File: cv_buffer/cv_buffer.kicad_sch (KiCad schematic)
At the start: 8 parts, among them J1 CV connector, J2 Pot connector, U1 HT7550-1, U2 TLV6001UIDBVR

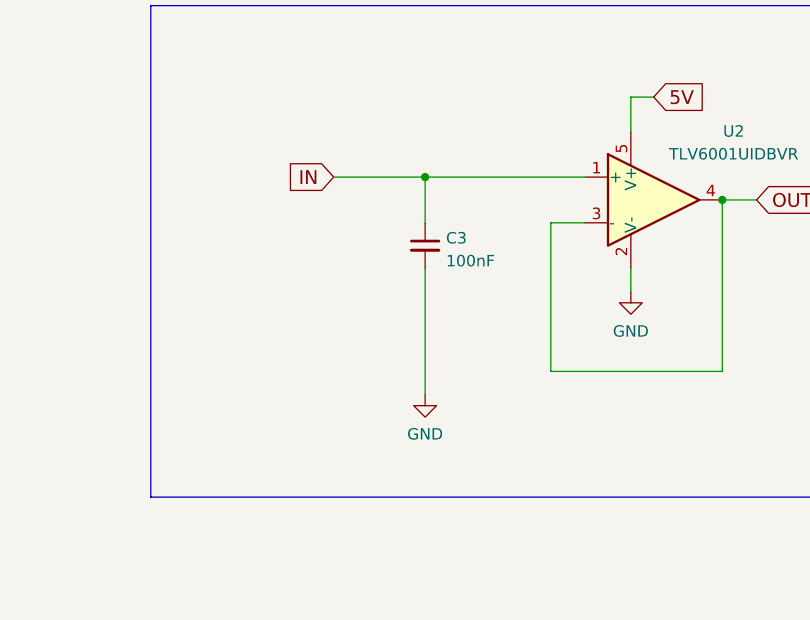
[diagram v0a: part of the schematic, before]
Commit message: - added tapering resistor - added fabrication script
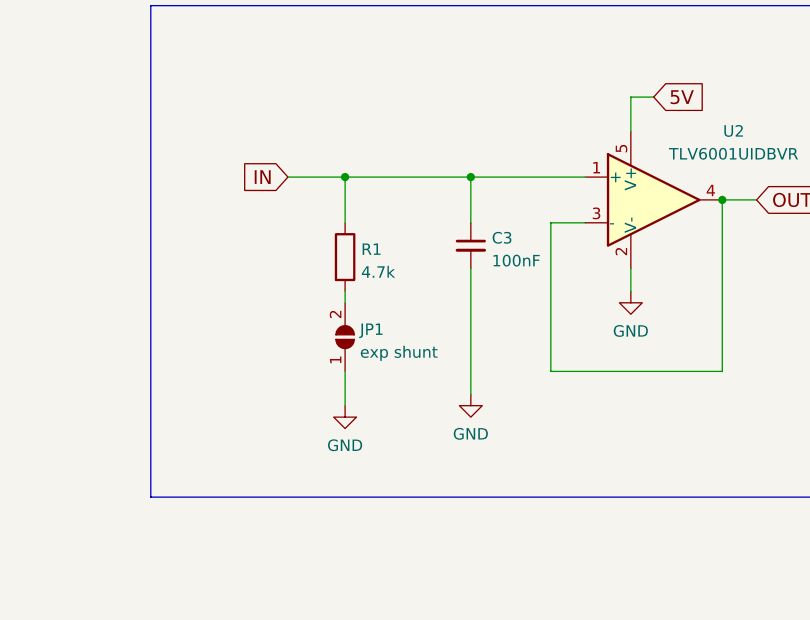
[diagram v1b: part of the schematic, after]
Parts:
- added JP1: exp shunt, Jumper:SolderJumper-2_P1.3mm_Open_TrianglePad1.0x1.5mm, symbol Jumper:SolderJumper_2_Open
- added R1: 4.7k, Resistor_SMD:R_0402_1005Metric, symbol Device:R
- U1: JLCPCB_CORRECTION (none) -> 0;0;180
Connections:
- net GND: now also JP1.1 (A)
- net IN: now also R1.1
- new net: JP1.2 (B), R1.2
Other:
- moved on the sheet: C3
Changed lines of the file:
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@@
   (junction (at 99.06 48.26) (diameter 0) (color 0 0 0 0)
   )
+  (junction (at 100.33 101.6) (diameter 0) (color 0 0 0 0)
+  )
   (junction (at 142.24 104.14) (diameter 0) (color 0 0 0 0)
   )
   (junction (at 120.65 59.69) (diameter 0) (color 0 0 0 0)
   )
-  (junction (at 109.22 101.6) (diameter 0) (color 0 0 0 0)
+  (junction (at 114.3 101.6) (diameter 0) (color 0 0 0 0)
   )
   (polyline (pts (xy 78.74 82.55) (xy 78.74 137.16))
@@
     (stroke (width 0) (type default) (color 0 0 0 0))
   )
+  (wire (pts (xy 100.33 101.6) (xy 100.33 106.68))
+    (stroke (width 0) (type default) (color 0 0 0 0))
+  )
   (polyline (pts (xy 179.07 82.55) (xy 217.17 82.55))
     (stroke (width 0) (type default) (color 0 0 0 0))
@@
     (stroke (width 0) (type default) (color 0 0 0 0))
   )
+  (wire (pts (xy 100.33 114.3) (xy 100.33 115.57))
+    (stroke (width 0) (type default) (color 0 0 0 0))
+  )
   (wire (pts (xy 120.65 48.26) (xy 120.65 52.07))
     (stroke (width 0) (type default) (color 0 0 0 0))
@@
     (stroke (width 0) (type default) (color 0 0 0 0))
   )
-  (wire (pts (xy 109.22 111.76) (xy 109.22 125.73))
+  (wire (pts (xy 114.3 111.76) (xy 114.3 125.73))
+    (stroke (width 0) (type default) (color 0 0 0 0))
+  )
+  (wire (pts (xy 100.33 123.19) (xy 100.33 127))
     (stroke (width 0) (type default) (color 0 0 0 0))
   )
@@
     (stroke (width 0) (type default) (color 0 0 0 0))
   )
-  (wire (pts (xy 109.22 101.6) (xy 127 101.6))
+  (wire (pts (xy 114.3 101.6) (xy 127 101.6))
     (stroke (width 0) (type default) (color 0 0 0 0))
   )
@@
     (stroke (width 0) (type default) (color 0 0 0 0))
   )
-  (wire (pts (xy 109.22 101.6) (xy 109.22 106.68))
+  (wire (pts (xy 114.3 101.6) (xy 114.3 106.68))
     (stroke (width 0) (type default) (color 0 0 0 0))
   )
@@
     (stroke (width 0) (type default) (color 0 0 0 0))
   )
+  (wire (pts (xy 100.33 101.6) (xy 114.3 101.6))
+    (stroke (width 0) (type default) (color 0 0 0 0))
+  )
   (wire (pts (xy 132.08 92.71) (xy 134.62 92.71))
     (stroke (width 0) (type default) (color 0 0 0 0))
@@
     (stroke (width 0) (type default) (color 0 0 0 0))
   )
-  (wire (pts (xy 99.06 101.6) (xy 109.22 101.6))
+  (wire (pts (xy 93.98 101.6) (xy 100.33 101.6))
     (stroke (width 0) (type default) (color 0 0 0 0))
   )
@@
     )
   )
-  (global_label "IN" (shape input) (at 99.06 101.6 180) (fields_autoplaced)
-    (effects (font (size 1.524 1.524)) (justify right))
-    (property "Intersheet References" "${INTERSHEET_REFS}" (id 0) (at 93.9488 101.5048 0)
+  (global_label "IN" (shape input) (at 93.98 101.6 180) (fields_autoplaced)
+    (effects (font (size 1.524 1.524)) (justify right))
+    (property "Intersheet References" "${INTERSHEET_REFS}" (id 0) (at 88.8688 101.5048 0)
       (effects (font (size 1.524 1.524)) (justify right) hide)
     )
@@
     (pin "1")
   )
+  (symbol (lib_id "Jumper:SolderJumper_2_Open") (at 100.33 119.38 90) (unit 1)
+    (in_bom yes) (on_board yes) (fields_autoplaced)
+    (property "Reference" "JP1" (id 0) (at 101.981 118.5453 90)
+      (effects (font (size 1.27 1.27)) (justify right))
+    )
+    (property "Value" "exp shunt" (id 1) (at 101.981 121.0822 90)
+      (effects (font (size 1.27 1.27)) (justify right))
+    )
+    (property "Footprint" "Jumper:SolderJumper-2_P1.3mm_Open_TrianglePad1.0x1.5mm" (id 2) (at 100.33 119.38 0)
+      (effects (font (size 1.27 1.27)) hide)
+    )
+    (property "Datasheet" "~" (id 3) (at 100.33 119.38 0)
+      (effects (font (size 1.27 1.27)) hide)
+    )
+    (pin "1")
+    (pin "2")
+  )
   (symbol (lib_id "power:PWR_FLAG") (at 124.46 59.69 180) (unit 1)
     (in_bom yes) (on_board yes) (fields_autoplaced)
@@
     (pin "1")
   )
-  (symbol (lib_id "power:GND") (at 109.22 125.73 0) (unit 1)
-    (in_bom yes) (on_board yes) (fields_autoplaced)
-    (property "Reference" "#PWR01" (id 0) (at 109.22 132.08 0)
-      (effects (font (size 1.27 1.27)) hide)
-    )
-    (property "Value" "GND" (id 1) (at 109.22 130.1734 0))
-    (property "Footprint" "" (id 2) (at 109.22 125.73 0)
-      (effects (font (size 1.27 1.27)) hide)
-    )
-    (property "Datasheet" "" (id 3) (at 109.22 125.73 0)
+  (symbol (lib_id "power:GND") (at 114.3 125.73 0) (unit 1)
+    (in_bom yes) (on_board yes) (fields_autoplaced)
+    (property "Reference" "#PWR01" (id 0) (at 114.3 132.08 0)
+      (effects (font (size 1.27 1.27)) hide)
+    )
+    (property "Value" "GND" (id 1) (at 114.3 130.1734 0))
+    (property "Footprint" "" (id 2) (at 114.3 125.73 0)
+      (effects (font (size 1.27 1.27)) hide)
+    )
+    (property "Datasheet" "" (id 3) (at 114.3 125.73 0)
       (effects (font (size 1.27 1.27)) hide)
     )
@@
     )
     (property "LCSC" "C15850" (id 4) (at 99.06 54.61 0)
+      (effects (font (size 1.524 1.524)) hide)
+    )
+    (pin "1")
+    (pin "2")
+  )
+  (symbol (lib_id "Device:R") (at 100.33 110.49 0) (unit 1)
+    (in_bom yes) (on_board yes) (fields_autoplaced)
+    (property "Reference" "R1" (id 0) (at 102.108 109.6553 0)
+      (effects (font (size 1.27 1.27)) (justify left))
+    )
+    (property "Value" "4.7k" (id 1) (at 102.108 112.1922 0)
+      (effects (font (size 1.27 1.27)) (justify left))
+    )
+    (property "Footprint" "Resistor_SMD:R_0402_1005Metric" (id 2) (at 98.552 110.49 90)
+      (effects (font (size 1.27 1.27)) hide)
+    )
+    (property "Datasheet" "~" (id 3) (at 100.33 110.49 0)
+      (effects (font (size 1.27 1.27)) hide)
+    )
+    (property "LCSC" "C25900" (id 4) (at 100.33 110.49 0)
       (effects (font (size 1.524 1.524)) hide)
     )
@@
       (effects (font (size 1.524 1.524)) hide)
     )
+    (property "JLCPCB_CORRECTION" "0;0;180" (id 5) (at 110.49 48.26 0)
+      (effects (font (size 1.524 1.524)) hide)
+    )
     (pin "1")
     (pin "2")
@@
     )
     (property "Datasheet" "~" (id 3) (at 99.06 44.45 0)
+      (effects (font (size 1.27 1.27)) hide)
+    )
+    (pin "1")
+  )
+  (symbol (lib_id "power:GND") (at 100.33 127 0) (unit 1)
+    (in_bom yes) (on_board yes) (fields_autoplaced)
+    (property "Reference" "#PWR03" (id 0) (at 100.33 133.35 0)
+      (effects (font (size 1.27 1.27)) hide)
+    )
+    (property "Value" "GND" (id 1) (at 100.33 131.4434 0))
+    (property "Footprint" "" (id 2) (at 100.33 127 0)
+      (effects (font (size 1.27 1.27)) hide)
+    )
+    (property "Datasheet" "" (id 3) (at 100.33 127 0)
       (effects (font (size 1.27 1.27)) hide)
     )
@@
     (pin "3")
   )
-  (symbol (lib_id "Device:C_Small") (at 109.22 109.22 0) (unit 1)
-    (in_bom yes) (on_board yes) (fields_autoplaced)
-    (property "Reference" "C3" (id 0) (at 111.5441 108.3916 0)
-      (effects (font (size 1.27 1.27)) (justify left))
-    )
-    (property "Value" "100nF" (id 1) (at 111.5441 110.9285 0)
-      (effects (font (size 1.27 1.27)) (justify left))
-    )
-    (property "Footprint" "Capacitor_SMD:C_0402_1005Metric" (id 2) (at 109.22 109.22 0)
-      (effects (font (size 1.27 1.27)) hide)
-    )
-    (property "Datasheet" "~" (id 3) (at 109.22 109.22 0)
-      (effects (font (size 1.27 1.27)) hide)
-    )
-    (property "LCSC" "C307331" (id 4) (at 109.22 109.22 0)
+  (symbol (lib_id "Device:C_Small") (at 114.3 109.22 0) (unit 1)
+    (in_bom yes) (on_board yes) (fields_autoplaced)
+    (property "Reference" "C3" (id 0) (at 116.6241 108.3916 0)
+      (effects (font (size 1.27 1.27)) (justify left))
+    )
+    (property "Value" "100nF" (id 1) (at 116.6241 110.9285 0)
+      (effects (font (size 1.27 1.27)) (justify left))
+    )
+    (property "Footprint" "Capacitor_SMD:C_0402_1005Metric" (id 2) (at 114.3 109.22 0)
+      (effects (font (size 1.27 1.27)) hide)
+    )
+    (property "Datasheet" "~" (id 3) (at 114.3 109.22 0)
+      (effects (font (size 1.27 1.27)) hide)
+    )
+    (property "LCSC" "C307331" (id 4) (at 114.3 109.22 0)
       (effects (font (size 1.524 1.524)) hide)
     )
@@
       (reference "#PWR02") (unit 1) (value "GND") (footprint "")
     )
+    (path "/c64623ea-1b89-43ec-92c6-a2d8ff19adad"
+      (reference "#PWR03") (unit 1) (value "GND") (footprint "")
+    )
     (path "/3e5b385e-4a64-4053-880e-e0031299a98c"
       (reference "#PWR05") (unit 1) (value "GND") (footprint "")
@@
       (reference "J2") (unit 1) (value "Pot connector") (footprint "cycfi_library:pin_header_1x3p_2.54mm_smd_horizontal")
     )
+    (path "/4d15044e-ba42-49c7-9385-a61cb67a80bd"
+      (reference "JP1") (unit 1) (value "exp shunt") (footprint "Jumper:SolderJumper-2_P1.3mm_Open_TrianglePad1.0x1.5mm")
+    )
+    (path "/92180a56-bc8d-4a49-8fe4-c3dc9309f11b"
+      (reference "R1") (unit 1) (value "4.7k") (footprint "Resistor_SMD:R_0402_1005Metric")
+    )
     (path "/b29e7a3c-8a61-4d5d-8478-053e45b60270"

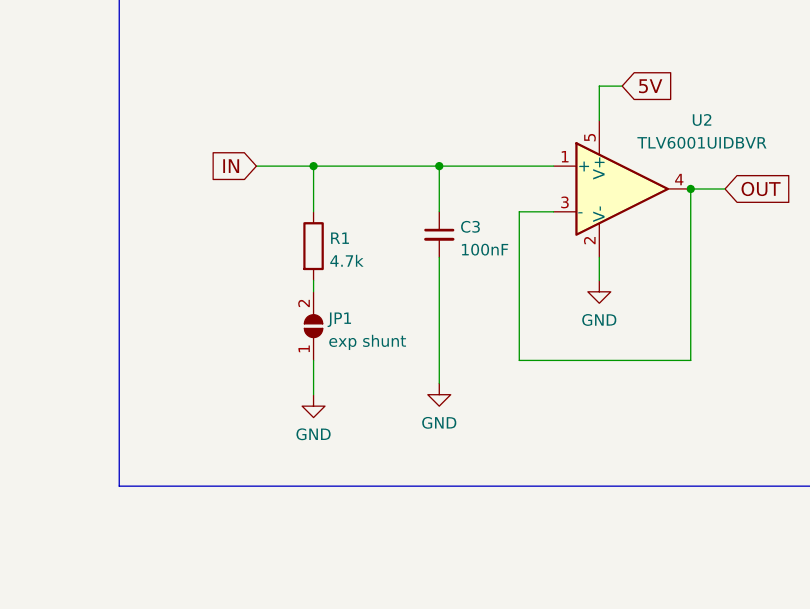
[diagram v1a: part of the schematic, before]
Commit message: Removed taper resistor
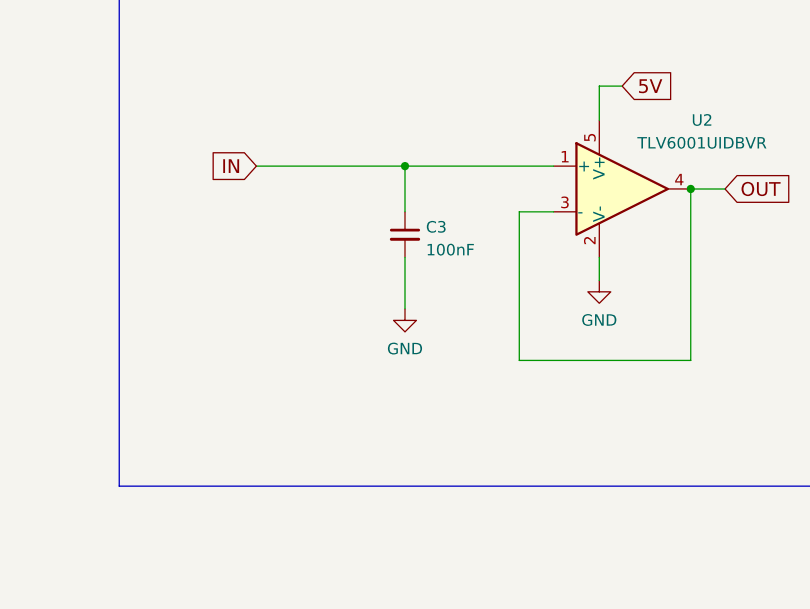
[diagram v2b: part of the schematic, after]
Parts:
- removed JP1: exp shunt, Jumper:SolderJumper-2_P1.3mm_Open_TrianglePad1.0x1.5mm, symbol Jumper:SolderJumper_2_Open
- removed R1: 4.7k, Resistor_SMD:R_0402_1005Metric, symbol Device:R
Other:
- moved on the sheet: C3
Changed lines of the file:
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@@
   (junction (at 99.06 48.26) (diameter 0) (color 0 0 0 0)
   )
-  (junction (at 100.33 101.6) (diameter 0) (color 0 0 0 0)
-  )
   (junction (at 142.24 104.14) (diameter 0) (color 0 0 0 0)
   )
   (junction (at 120.65 59.69) (diameter 0) (color 0 0 0 0)
   )
-  (junction (at 114.3 101.6) (diameter 0) (color 0 0 0 0)
+  (junction (at 110.49 101.6) (diameter 0) (color 0 0 0 0)
   )
   (polyline (pts (xy 78.74 82.55) (xy 78.74 137.16))
@@
     (stroke (width 0) (type default) (color 0 0 0 0))
   )
-  (wire (pts (xy 100.33 101.6) (xy 100.33 106.68))
-    (stroke (width 0) (type default) (color 0 0 0 0))
-  )
   (polyline (pts (xy 179.07 82.55) (xy 217.17 82.55))
     (stroke (width 0) (type default) (color 0 0 0 0))
@@
     (stroke (width 0) (type default) (color 0 0 0 0))
   )
-  (wire (pts (xy 100.33 114.3) (xy 100.33 115.57))
-    (stroke (width 0) (type default) (color 0 0 0 0))
-  )
   (wire (pts (xy 120.65 48.26) (xy 120.65 52.07))
     (stroke (width 0) (type default) (color 0 0 0 0))
@@
     (stroke (width 0) (type default) (color 0 0 0 0))
   )
-  (wire (pts (xy 114.3 111.76) (xy 114.3 125.73))
-    (stroke (width 0) (type default) (color 0 0 0 0))
-  )
-  (wire (pts (xy 100.33 123.19) (xy 100.33 127))
+  (wire (pts (xy 110.49 111.76) (xy 110.49 117.475))
     (stroke (width 0) (type default) (color 0 0 0 0))
   )
@@
     (stroke (width 0) (type default) (color 0 0 0 0))
   )
-  (wire (pts (xy 114.3 101.6) (xy 127 101.6))
+  (wire (pts (xy 110.49 101.6) (xy 127 101.6))
     (stroke (width 0) (type default) (color 0 0 0 0))
   )
@@
     (stroke (width 0) (type default) (color 0 0 0 0))
   )
-  (wire (pts (xy 114.3 101.6) (xy 114.3 106.68))
+  (wire (pts (xy 110.49 101.6) (xy 110.49 106.68))
     (stroke (width 0) (type default) (color 0 0 0 0))
   )
@@
     (stroke (width 0) (type default) (color 0 0 0 0))
   )
-  (wire (pts (xy 100.33 101.6) (xy 114.3 101.6))
+  (wire (pts (xy 93.98 101.6) (xy 110.49 101.6))
     (stroke (width 0) (type default) (color 0 0 0 0))
   )
@@
   )
   (polyline (pts (xy 138.43 35.56) (xy 138.43 73.66))
-    (stroke (width 0) (type default) (color 0 0 0 0))
-  )
-  (wire (pts (xy 93.98 101.6) (xy 100.33 101.6))
     (stroke (width 0) (type default) (color 0 0 0 0))
   )
@@
     (pin "1")
   )
-  (symbol (lib_id "Jumper:SolderJumper_2_Open") (at 100.33 119.38 90) (unit 1)
-    (in_bom yes) (on_board yes) (fields_autoplaced)
-    (property "Reference" "JP1" (id 0) (at 101.981 118.5453 90)
-      (effects (font (size 1.27 1.27)) (justify right))
-    )
-    (property "Value" "exp shunt" (id 1) (at 101.981 121.0822 90)
-      (effects (font (size 1.27 1.27)) (justify right))
-    )
-    (property "Footprint" "Jumper:SolderJumper-2_P1.3mm_Open_TrianglePad1.0x1.5mm" (id 2) (at 100.33 119.38 0)
-      (effects (font (size 1.27 1.27)) hide)
-    )
-    (property "Datasheet" "~" (id 3) (at 100.33 119.38 0)
-      (effects (font (size 1.27 1.27)) hide)
-    )
-    (pin "1")
-    (pin "2")
-  )
   (symbol (lib_id "power:PWR_FLAG") (at 124.46 59.69 180) (unit 1)
     (in_bom yes) (on_board yes) (fields_autoplaced)
@@
     (pin "1")
   )
-  (symbol (lib_id "power:GND") (at 114.3 125.73 0) (unit 1)
-    (in_bom yes) (on_board yes) (fields_autoplaced)
-    (property "Reference" "#PWR01" (id 0) (at 114.3 132.08 0)
-      (effects (font (size 1.27 1.27)) hide)
-    )
-    (property "Value" "GND" (id 1) (at 114.3 130.1734 0))
-    (property "Footprint" "" (id 2) (at 114.3 125.73 0)
-      (effects (font (size 1.27 1.27)) hide)
-    )
-    (property "Datasheet" "" (id 3) (at 114.3 125.73 0)
+  (symbol (lib_id "power:GND") (at 110.49 117.475 0) (unit 1)
+    (in_bom yes) (on_board yes) (fields_autoplaced)
+    (property "Reference" "#PWR01" (id 0) (at 110.49 123.825 0)
+      (effects (font (size 1.27 1.27)) hide)
+    )
+    (property "Value" "GND" (id 1) (at 110.49 121.9184 0))
+    (property "Footprint" "" (id 2) (at 110.49 117.475 0)
+      (effects (font (size 1.27 1.27)) hide)
+    )
+    (property "Datasheet" "" (id 3) (at 110.49 117.475 0)
       (effects (font (size 1.27 1.27)) hide)
     )
@@
     )
     (property "LCSC" "C15850" (id 4) (at 99.06 54.61 0)
-      (effects (font (size 1.524 1.524)) hide)
-    )
-    (pin "1")
-    (pin "2")
-  )
-  (symbol (lib_id "Device:R") (at 100.33 110.49 0) (unit 1)
-    (in_bom yes) (on_board yes) (fields_autoplaced)
-    (property "Reference" "R1" (id 0) (at 102.108 109.6553 0)
-      (effects (font (size 1.27 1.27)) (justify left))
-    )
-    (property "Value" "4.7k" (id 1) (at 102.108 112.1922 0)
-      (effects (font (size 1.27 1.27)) (justify left))
-    )
-    (property "Footprint" "Resistor_SMD:R_0402_1005Metric" (id 2) (at 98.552 110.49 90)
-      (effects (font (size 1.27 1.27)) hide)
-    )
-    (property "Datasheet" "~" (id 3) (at 100.33 110.49 0)
-      (effects (font (size 1.27 1.27)) hide)
-    )
-    (property "LCSC" "C25900" (id 4) (at 100.33 110.49 0)
       (effects (font (size 1.524 1.524)) hide)
     )
@@
     )
     (property "Datasheet" "~" (id 3) (at 99.06 44.45 0)
-      (effects (font (size 1.27 1.27)) hide)
-    )
-    (pin "1")
-  )
-  (symbol (lib_id "power:GND") (at 100.33 127 0) (unit 1)
-    (in_bom yes) (on_board yes) (fields_autoplaced)
-    (property "Reference" "#PWR03" (id 0) (at 100.33 133.35 0)
-      (effects (font (size 1.27 1.27)) hide)
-    )
-    (property "Value" "GND" (id 1) (at 100.33 131.4434 0))
-    (property "Footprint" "" (id 2) (at 100.33 127 0)
-      (effects (font (size 1.27 1.27)) hide)
-    )
-    (property "Datasheet" "" (id 3) (at 100.33 127 0)
       (effects (font (size 1.27 1.27)) hide)
     )
@@
     (pin "3")
   )
-  (symbol (lib_id "Device:C_Small") (at 114.3 109.22 0) (unit 1)
-    (in_bom yes) (on_board yes) (fields_autoplaced)
-    (property "Reference" "C3" (id 0) (at 116.6241 108.3916 0)
-      (effects (font (size 1.27 1.27)) (justify left))
-    )
-    (property "Value" "100nF" (id 1) (at 116.6241 110.9285 0)
-      (effects (font (size 1.27 1.27)) (justify left))
-    )
-    (property "Footprint" "Capacitor_SMD:C_0402_1005Metric" (id 2) (at 114.3 109.22 0)
-      (effects (font (size 1.27 1.27)) hide)
-    )
-    (property "Datasheet" "~" (id 3) (at 114.3 109.22 0)
-      (effects (font (size 1.27 1.27)) hide)
-    )
-    (property "LCSC" "C307331" (id 4) (at 114.3 109.22 0)
+  (symbol (lib_id "Device:C_Small") (at 110.49 109.22 0) (unit 1)
+    (in_bom yes) (on_board yes) (fields_autoplaced)
+    (property "Reference" "C3" (id 0) (at 112.8141 108.3916 0)
+      (effects (font (size 1.27 1.27)) (justify left))
+    )
+    (property "Value" "100nF" (id 1) (at 112.8141 110.9285 0)
+      (effects (font (size 1.27 1.27)) (justify left))
+    )
+    (property "Footprint" "Capacitor_SMD:C_0402_1005Metric" (id 2) (at 110.49 109.22 0)
+      (effects (font (size 1.27 1.27)) hide)
+    )
+    (property "Datasheet" "~" (id 3) (at 110.49 109.22 0)
+      (effects (font (size 1.27 1.27)) hide)
+    )
+    (property "LCSC" "C307331" (id 4) (at 110.49 109.22 0)
       (effects (font (size 1.524 1.524)) hide)
     )
@@
       (reference "#PWR02") (unit 1) (value "GND") (footprint "")
     )
-    (path "/c64623ea-1b89-43ec-92c6-a2d8ff19adad"
-      (reference "#PWR03") (unit 1) (value "GND") (footprint "")
-    )
     (path "/3e5b385e-4a64-4053-880e-e0031299a98c"
       (reference "#PWR05") (unit 1) (value "GND") (footprint "")
@@
       (reference "J2") (unit 1) (value "Pot connector") (footprint "cycfi_library:pin_header_1x3p_2.54mm_smd_horizontal")
     )
-    (path "/4d15044e-ba42-49c7-9385-a61cb67a80bd"
-      (reference "JP1") (unit 1) (value "exp shunt") (footprint "Jumper:SolderJumper-2_P1.3mm_Open_TrianglePad1.0x1.5mm")
-    )
-    (path "/92180a56-bc8d-4a49-8fe4-c3dc9309f11b"
-      (reference "R1") (unit 1) (value "4.7k") (footprint "Resistor_SMD:R_0402_1005Metric")
-    )
     (path "/b29e7a3c-8a61-4d5d-8478-053e45b60270"

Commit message: Added rotation correction for JLCPCB
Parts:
- U2: JLCPCB_CORRECTION (none) -> 0;0;180
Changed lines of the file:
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@@
+      (effects (font (size 1.27 1.27)) hide)
+    )
+    (property "JLCPCB_CORRECTION" "0;0;180" (id 4) (at 134.62 104.14 0)
       (effects (font (size 1.27 1.27)) hide)
     )
